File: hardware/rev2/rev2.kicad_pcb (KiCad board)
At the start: 2 copper layers, 24 parts, among them J1 Conn_01x09_Female, J2 RFM9X_header, J3 Conn_02x03_Odd_Even, U2 MPL3115A2, U3 Teensy3.6, U5 ADXL345BCCZ, U7 TPS2113ADRBR

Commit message: update netlist
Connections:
- U3 pad 11: MAIN_DEPLOY -> INT1_ADXL345
- U3 pad 12: DROGUE_DEPLOY -> INT2_ADXL345
- U3 pad 2: INT1_ADXL345 -> Net-(U3-Pad2)
- U3 pad 21: BUZZER -> INT1_MPL3115A2
- U3 pad 22: Net-(U3-Pad22) -> INT2_MPL3115A2
- U3 pad 3: INT2_ADXL345 -> Net-(U3-Pad3)
- U3 pad 35: Net-(U3-Pad35) -> BUZZER
- U3 pad 5: SCL_TEENSY -> Net-(U3-Pad5)
- U3 pad 6: SDA_TEENSY -> Net-(U3-Pad6)
- U3 pad 7: INT1_MPL3115A2 -> MAIN_DEPLOY
- U3 pad 8: INT2_MPL3115A2 -> DROGUE_DEPLOY
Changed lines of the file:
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@@
     (zones 0)
     (modules 24)
-    (nets 73)
+    (nets 75)
   )
   (page A4)
@@
   (net 55 "Net-(J1-Pad7)")
   (net 56 "Net-(J1-Pad9)")
-  (net 57 "Net-(U3-Pad35)")
-  (net 58 MAIN_DEPLOY)
-  (net 59 DROGUE_DEPLOY)
-  (net 60 3.3VBMS_Backup)
-  (net 61 "Net-(J3-Pad6)")
-  (net 62 BUZZER)
-  (net 63 "Net-(R5-Pad1)")
-  (net 64 "Net-(R7-Pad2)")
-  (net 65 "Net-(U3-Pad18)")
-  (net 66 "Net-(U3-Pad19)")
-  (net 67 "Net-(U3-Pad22)")
-  (net 68 "Net-(U3-Pad23)")
-  (net 69 "Net-(U3-Pad24)")
-  (net 70 "Net-(U3-Pad10)")
-  (net 71 "Net-(U3-Pad9)")
-  (net 72 "Net-(U7-Pad1)")
+  (net 57 MAIN_DEPLOY)
+  (net 58 DROGUE_DEPLOY)
+  (net 59 3.3VBMS_Backup)
+  (net 60 "Net-(J3-Pad6)")
+  (net 61 BUZZER)
+  (net 62 "Net-(R5-Pad1)")
+  (net 63 "Net-(R7-Pad2)")
+  (net 64 "Net-(U3-Pad18)")
+  (net 65 "Net-(U3-Pad19)")
+  (net 66 "Net-(U3-Pad23)")
+  (net 67 "Net-(U3-Pad24)")
+  (net 68 "Net-(U3-Pad10)")
+  (net 69 "Net-(U3-Pad9)")
+  (net 70 "Net-(U7-Pad1)")
+  (net 71 "Net-(U3-Pad6)")
+  (net 72 "Net-(U3-Pad5)")
+  (net 73 "Net-(U3-Pad3)")
+  (net 74 "Net-(U3-Pad2)")
   (net_class Default "This is the default net class."
     (clearance 0.2)
@@
     (add_net "Net-(U3-Pad18)")
     (add_net "Net-(U3-Pad19)")
+    (add_net "Net-(U3-Pad2)")
     (add_net "Net-(U3-Pad20)")
-    (add_net "Net-(U3-Pad22)")
     (add_net "Net-(U3-Pad23)")
     (add_net "Net-(U3-Pad24)")
@@
     (add_net "Net-(U3-Pad28)")
     (add_net "Net-(U3-Pad29)")
-    (add_net "Net-(U3-Pad35)")
+    (add_net "Net-(U3-Pad3)")
     (add_net "Net-(U3-Pad36)")
     (add_net "Net-(U3-Pad37)")
@@
     (add_net "Net-(U3-Pad47)")
     (add_net "Net-(U3-Pad48)")
+    (add_net "Net-(U3-Pad5)")
     (add_net "Net-(U3-Pad51)")
     (add_net "Net-(U3-Pad52)")
@@
     (add_net "Net-(U3-Pad56)")
     (add_net "Net-(U3-Pad57)")
+    (add_net "Net-(U3-Pad6)")
     (add_net "Net-(U3-Pad9)")
     (add_net "Net-(U5-Pad10)")
@@
       (net 29 "Net-(U3-Pad17)"))
     (pad 18 thru_hole circle (at 13.97 7.62) (size 1.6 1.6) (drill 1.1) (layers *.Cu *.Mask)
-      (net 65 "Net-(U3-Pad18)"))
+      (net 64 "Net-(U3-Pad18)"))
     (pad 19 thru_hole circle (at 16.51 7.62) (size 1.6 1.6) (drill 1.1) (layers *.Cu *.Mask)
-      (net 66 "Net-(U3-Pad19)"))
+      (net 65 "Net-(U3-Pad19)"))
     (pad 20 thru_hole circle (at 19.05 7.62) (size 1.6 1.6) (drill 1.1) (layers *.Cu *.Mask)
       (net 7 "Net-(U3-Pad20)"))
@@
       (net 43 MISO_RFM9X))
     (pad 21 thru_hole circle (at 21.59 7.62) (size 1.6 1.6) (drill 1.1) (layers *.Cu *.Mask)
-      (net 62 BUZZER))
+      (net 6 INT1_MPL3115A2))
     (pad 22 thru_hole circle (at 24.13 7.62) (size 1.6 1.6) (drill 1.1) (layers *.Cu *.Mask)
-      (net 67 "Net-(U3-Pad22)"))
+      (net 5 INT2_MPL3115A2))
     (pad 23 thru_hole circle (at 26.67 7.62) (size 1.6 1.6) (drill 1.1) (layers *.Cu *.Mask)
-      (net 68 "Net-(U3-Pad23)"))
+      (net 66 "Net-(U3-Pad23)"))
     (pad 24 thru_hole circle (at 29.21 7.62) (size 1.6 1.6) (drill 1.1) (layers *.Cu *.Mask)
-      (net 69 "Net-(U3-Pad24)"))
+      (net 67 "Net-(U3-Pad24)"))
     (pad 25 thru_hole circle (at 16.51 5.08) (size 1.6 1.6) (drill 1.1) (layers *.Cu *.Mask)
       (net 8 "Net-(U3-Pad25)"))
@@
       (net 34 PPS))
     (pad 35 thru_hole circle (at 16.51 -7.62) (size 1.6 1.6) (drill 1.1) (layers *.Cu *.Mask)
-      (net 57 "Net-(U3-Pad35)"))
+      (net 61 BUZZER))
     (pad 36 thru_hole circle (at 13.97 -7.62) (size 1.6 1.6) (drill 1.1) (layers *.Cu *.Mask)
       (net 13 "Net-(U3-Pad36)"))
@@
       (net 44 MOSI_RFM9X))
     (pad 12 thru_hole circle (at -1.27 7.62) (size 1.6 1.6) (drill 1.1) (layers *.Cu *.Mask)
-      (net 59 DROGUE_DEPLOY))
+      (net 36 INT2_ADXL345))
     (pad 11 thru_hole circle (at -3.81 7.62) (size 1.6 1.6) (drill 1.1) (layers *.Cu *.Mask)
-      (net 58 MAIN_DEPLOY))
+      (net 37 INT1_ADXL345))
     (pad 10 thru_hole circle (at -6.35 7.62) (size 1.6 1.6) (drill 1.1) (layers *.Cu *.Mask)
-      (net 70 "Net-(U3-Pad10)"))
+      (net 68 "Net-(U3-Pad10)"))
     (pad 9 thru_hole circle (at -8.89 7.62) (size 1.6 1.6) (drill 1.1) (layers *.Cu *.Mask)
-      (net 71 "Net-(U3-Pad9)"))
+      (net 69 "Net-(U3-Pad9)"))
     (pad 8 thru_hole circle (at -11.43 7.62) (size 1.6 1.6) (drill 1.1) (layers *.Cu *.Mask)
-      (net 5 INT2_MPL3115A2))
+      (net 58 DROGUE_DEPLOY))
     (pad 7 thru_hole circle (at -13.97 7.62) (size 1.6 1.6) (drill 1.1) (layers *.Cu *.Mask)
-      (net 6 INT1_MPL3115A2))
+      (net 57 MAIN_DEPLOY))
     (pad 6 thru_hole circle (at -16.51 7.62) (size 1.6 1.6) (drill 1.1) (layers *.Cu *.Mask)
-      (net 3 SDA_TEENSY))
+      (net 71 "Net-(U3-Pad6)"))
     (pad 5 thru_hole circle (at -19.05 7.62) (size 1.6 1.6) (drill 1.1) (layers *.Cu *.Mask)
-      (net 4 SCL_TEENSY))
+      (net 72 "Net-(U3-Pad5)"))
     (pad 4 thru_hole circle (at -21.59 7.62) (size 1.6 1.6) (drill 1.1) (layers *.Cu *.Mask)
       (net 41 G0_RFM9X))
     (pad 3 thru_hole circle (at -24.13 7.62) (size 1.6 1.6) (drill 1.1) (layers *.Cu *.Mask)
-      (net 36 INT2_ADXL345))
+      (net 73 "Net-(U3-Pad3)"))
     (pad 2 thru_hole circle (at -26.67 7.62) (size 1.6 1.6) (drill 1.1) (layers *.Cu *.Mask)
-      (net 37 INT1_ADXL345))
+      (net 74 "Net-(U3-Pad2)"))
     (pad 1 thru_hole rect (at -29.21 7.62) (size 1.6 1.6) (drill 1.1) (layers *.Cu *.Mask)
       (net 1 GND))
@@
     (fp_line (start -1 0.62) (end -1 -0.62) (layer F.Fab) (width 0.1))
     (pad 1 smd rect (at -0.95 0 270) (size 0.7 1.3) (layers F.Cu F.Paste F.Mask)
-      (net 63 "Net-(R5-Pad1)"))
+      (net 62 "Net-(R5-Pad1)"))
     (pad 2 smd rect (at 0.95 0 270) (size 0.7 1.3) (layers F.Cu F.Paste F.Mask)
       (net 52 3.3VBMS))
@@
       (net 1 GND))
     (pad P thru_hole circle (at 7.5 0) (size 1.71 1.71) (drill 1.14) (layers *.Cu *.Mask)
-      (net 62 BUZZER))
+      (net 61 BUZZER))
   )
   (module footprints:R_0805_OEM (layer F.Cu)
@@
       (net 1 GND))
     (pad 2 smd rect (at 0.95 0) (size 0.7 1.3) (layers F.Cu F.Paste F.Mask)
-      (net 63 "Net-(R5-Pad1)"))
+      (net 62 "Net-(R5-Pad1)"))
     (model "/home/josh/Formula/OEM_Preferred_Parts/3DModels/WRL Files/res0805.wrl"
       (at (xyz 0 0 0))
@@
     (fp_line (start 1.55 0.9) (end -1.55 0.9) (layer F.CrtYd) (width 0.05))
     (pad 2 smd rect (at 0.95 0) (size 0.7 1.3) (layers F.Cu F.Paste F.Mask)
-      (net 64 "Net-(R7-Pad2)"))
+      (net 63 "Net-(R7-Pad2)"))
     (pad 1 smd rect (at -0.95 0) (size 0.7 1.3) (layers F.Cu F.Paste F.Mask)
       (net 1 GND))
@@
       (net 54 BMS_to_Teensy))
     (pad 6 smd rect (at 1.4 0.325) (size 0.6 0.31) (layers F.Cu F.Paste)
-      (net 60 3.3VBMS_Backup))
+      (net 59 3.3VBMS_Backup))
     (pad 5 smd rect (at 1.4 0.975) (size 0.6 0.31) (layers F.Cu F.Paste)
       (net 1 GND))
     (pad 4 smd rect (at -1.4 0.975) (size 0.6 0.31) (layers F.Cu F.Paste)
-      (net 64 "Net-(R7-Pad2)"))
+      (net 63 "Net-(R7-Pad2)"))
     (pad 3 smd rect (at -1.4 0.325) (size 0.6 0.31) (layers F.Cu F.Paste)
-      (net 63 "Net-(R5-Pad1)"))
+      (net 62 "Net-(R5-Pad1)"))
     (pad 2 smd rect (at -1.4 -0.325) (size 0.6 0.31) (layers F.Cu F.Paste)
       (net 1 GND))
     (pad 1 smd rect (at -1.4 -0.975) (size 0.6 0.31) (layers F.Cu F.Paste)
-      (net 72 "Net-(U7-Pad1)"))
+      (net 70 "Net-(U7-Pad1)"))
   )
   (module Connector_PinHeader_2.54mm:PinHeader_2x03_P2.54mm_Vertical (layer F.Cu)
@@
       (net 1 GND))
     (pad 2 thru_hole oval (at 2.54 0 270) (size 1.7 1.7) (drill 1) (layers *.Cu *.Mask)
-      (net 58 MAIN_DEPLOY))
+      (net 57 MAIN_DEPLOY))
     (pad 3 thru_hole oval (at 0 2.54 270) (size 1.7 1.7) (drill 1) (layers *.Cu *.Mask)
       (net 52 3.3VBMS))
     (pad 4 thru_hole oval (at 2.54 2.54 270) (size 1.7 1.7) (drill 1) (layers *.Cu *.Mask)
-      (net 59 DROGUE_DEPLOY))
+      (net 58 DROGUE_DEPLOY))
     (pad 5 thru_hole oval (at 0 5.08 270) (size 1.7 1.7) (drill 1) (layers *.Cu *.Mask)
-      (net 60 3.3VBMS_Backup))
+      (net 59 3.3VBMS_Backup))
     (pad 6 thru_hole oval (at 2.54 5.08 270) (size 1.7 1.7) (drill 1) (layers *.Cu *.Mask)
-      (net 61 "Net-(J3-Pad6)"))
+      (net 60 "Net-(J3-Pad6)"))
     (model ${KISYS3DMOD}/Connector_PinHeader_2.54mm.3dshapes/PinHeader_2x03_P2.54mm_Vertical.wrl
       (at (xyz 0 0 0))
@@
   (via (at 154.7876 105.6132) (size 0.8) (drill 0.4) (layers F.Cu B.Cu) (net 4))
   (segment (start 154.7774 105.603) (end 154.7876 105.6132) (width 0.25) (layer F.Cu) (net 4))
-  (segment (start 133.223 102.8954) (end 133.223 102.616) (width 0.25) (layer B.Cu) (net 5) (status C00030))
+  (segment (start 133.223 102.8954) (end 133.223 102.616) (width 0.25) (layer B.Cu) (net 58) (status C00030))
   (segment (start 162.56 82.296) (end 164.846 84.582) (width 0.25) (layer F.Cu) (net 31) (status 400000))
   (segment (start 168.529 84.582) (end 171.323 87.376) (width 0.25) (layer F.Cu) (net 31) (status 800000))
@@
   (segment (start 166.751 85.09) (end 168.783 87.122) (width 0.25) (layer F.Cu) (net 35))
   (segment (start 162.814 85.09) (end 166.751 85.09) (width 0.25) (layer F.Cu) (net 35))
-  (segment (start 135.697 102.682) (end 135.763 102.616) (width 0.25) (layer B.Cu) (net 71) (status C00030))
+  (segment (start 135.697 102.682) (end 135.763 102.616) (width 0.25) (layer B.Cu) (net 69) (status C00030))
   (segment (start 118.491 82.042) (end 120.65 79.883) (width 0.25) (layer F.Cu) (net 40) (status 400010))
   (segment (start 138.43 79.883) (end 145.923 87.376) (width 0.25) (layer F.Cu) (net 40) (status 800020))

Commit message: wip
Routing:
- net GND: track 24.9 -> 42.1 mm, vias 2 -> 4
- net INT1_ADXL345: track 0.00 -> 14.2 mm, vias 0 -> 1
- net INT2_ADXL345: track 0.00 -> 11.8 mm, vias 0 -> 1
- net INT2_MPL3115A2: track 0.00 -> 6.16 mm
- net INT1_MPL3115A2: track 0.00 -> 5.62 mm
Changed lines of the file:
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@@
     (thickness 1.6)
     (drawings 18)
-    (tracks 115)
+    (tracks 143)
     (zones 0)
     (modules 24)
@@
   (segment (start 157.6451 113.8903) (end 153.7081 113.8903) (width 1) (layer F.Cu) (net 1) (status C00030))
   (segment (start 163.6549 109.4179) (end 163.6549 111.0461) (width 1) (layer F.Cu) (net 1) (status 400010))
+  (segment (start 163.6395 113.8809) (end 163.6268 113.8936) (width 1) (layer B.Cu) (net 1))
+  (segment (start 163.6395 111.0615) (end 163.6395 113.8809) (width 1) (layer B.Cu) (net 1))
+  (via (at 163.6268 113.8936) (size 1.2) (drill 0.6) (layers F.Cu B.Cu) (net 1))
+  (segment (start 163.6108 113.8776) (end 163.6268 113.8936) (width 1) (layer F.Cu) (net 1))
+  (segment (start 163.6108 113.8776) (end 161.5821 113.8903) (width 1) (layer F.Cu) (net 1) (status 800010))
+  (via (at 163.6395 111.0615) (size 1.2) (drill 0.6) (layers F.Cu B.Cu) (net 1))
   (segment (start 163.6549 111.0461) (end 163.6395 111.0615) (width 1) (layer F.Cu) (net 1))
-  (via (at 163.6395 111.0615) (size 1.2) (drill 0.6) (layers F.Cu B.Cu) (net 1))
-  (segment (start 161.5821 113.8903) (end 163.8521 113.8903) (width 1) (layer F.Cu) (net 1) (status 400010))
-  (segment (start 163.8521 113.8903) (end 163.8681 113.9063) (width 1) (layer F.Cu) (net 1))
-  (via (at 163.8681 113.9063) (size 1.2) (drill 0.6) (layers F.Cu B.Cu) (net 1))
   (segment (start 144.9545 110.5695) (end 144.78 110.744) (width 1) (layer F.Cu) (net 1))
   (segment (start 144.78 110.744) (end 144.9705 110.5535) (width 1) (layer F.Cu) (net 1))
@@
   (segment (start 142.891 110.744) (end 142.875 110.76) (width 1) (layer F.Cu) (net 1) (status C00000))
   (segment (start 142.875 110.76) (end 139.7 110.76) (width 1) (layer F.Cu) (net 1) (status C00000))
+  (segment (start 148.0125 108.3375) (end 148.9775 108.3375) (width 0.55) (layer F.Cu) (net 1) (status 400000))
+  (segment (start 151.5364 113.8936) (end 151.5397 113.8903) (width 0.55) (layer F.Cu) (net 1))
+  (via (at 151.5364 113.8936) (size 1.2) (drill 0.6) (layers F.Cu B.Cu) (net 1))
+  (segment (start 151.5364 109.728) (end 151.5364 113.8936) (width 0.55) (layer B.Cu) (net 1))
+  (via (at 150.622 108.8136) (size 1.2) (drill 0.6) (layers F.Cu B.Cu) (net 1))
+  (segment (start 149.4536 108.8136) (end 150.622 108.8136) (width 0.55) (layer F.Cu) (net 1))
+  (segment (start 148.9775 108.3375) (end 149.4536 108.8136) (width 0.55) (layer F.Cu) (net 1))
+  (segment (start 153.7081 113.8903) (end 151.5397 113.8903) (width 1) (layer F.Cu) (net 1) (status 400000))
+  (segment (start 151.5397 113.8903) (end 151.5364 113.8936) (width 1) (layer F.Cu) (net 1))
+  (segment (start 150.622 108.8136) (end 151.5364 109.728) (width 1) (layer B.Cu) (net 1))
+  (segment (start 151.5364 109.728) (end 151.5364 113.8936) (width 1) (layer B.Cu) (net 1))
   (segment (start 161.5821 112.2553) (end 167.1701 112.2553) (width 0.25) (layer F.Cu) (net 2) (status 10))
   (segment (start 169.5196 112.2553) (end 169.9006 112.6363) (width 0.25) (layer F.Cu) (net 2) (status C00030))
@@
   (via (at 154.7876 105.6132) (size 0.8) (drill 0.4) (layers F.Cu B.Cu) (net 4))
   (segment (start 154.7774 105.603) (end 154.7876 105.6132) (width 0.25) (layer F.Cu) (net 4))
+  (segment (start 164.9049 107.1679) (end 164.9049 106.4941) (width 0.25) (layer F.Cu) (net 5) (status 400000))
+  (segment (start 164.9049 106.4941) (end 168.783 102.616) (width 0.25) (layer F.Cu) (net 5) (status 800000))
+  (segment (start 163.6549 107.1679) (end 163.6549 105.2041) (width 0.25) (layer F.Cu) (net 6) (status 400000))
+  (segment (start 163.6549 105.2041) (end 166.243 102.616) (width 0.25) (layer F.Cu) (net 6) (status 800000))
   (segment (start 133.223 102.8954) (end 133.223 102.616) (width 0.25) (layer B.Cu) (net 58) (status C00030))
   (segment (start 162.56 82.296) (end 164.846 84.582) (width 0.25) (layer F.Cu) (net 31) (status 400000))
@@
   (segment (start 166.751 85.09) (end 168.783 87.122) (width 0.25) (layer F.Cu) (net 35))
   (segment (start 162.814 85.09) (end 166.751 85.09) (width 0.25) (layer F.Cu) (net 35))
+  (segment (start 148.0125 110.7375) (end 148.7489 110.7375) (width 0.25) (layer F.Cu) (net 36) (status 400000))
+  (segment (start 149.606 108.839) (end 143.383 102.616) (width 0.25) (layer B.Cu) (net 36) (status 800000))
+  (segment (start 149.606 109.8296) (end 149.606 108.839) (width 0.25) (layer B.Cu) (net 36))
+  (segment (start 148.7489 110.7375) (end 149.606 109.8804) (width 0.25) (layer F.Cu) (net 36))
+  (segment (start 149.606 109.8804) (end 149.606 109.8296) (width 0.25) (layer F.Cu) (net 36))
+  (via (at 149.606 109.8296) (size 0.8) (drill 0.4) (layers F.Cu B.Cu) (net 36))
+  (segment (start 148.0125 111.5375) (end 149.3205 111.5375) (width 0.25) (layer F.Cu) (net 37) (status 400000))
+  (segment (start 141.0716 102.616) (end 140.843 102.616) (width 0.25) (layer B.Cu) (net 37) (status C00000))
+  (segment (start 149.6568 111.2012) (end 141.0716 102.616) (width 0.25) (layer B.Cu) (net 37) (status 800000))
+  (via (at 149.6568 111.2012) (size 0.8) (drill 0.4) (layers F.Cu B.Cu) (net 37))
+  (segment (start 149.3205 111.5375) (end 149.6568 111.2012) (width 0.25) (layer F.Cu) (net 37))
   (segment (start 135.697 102.682) (end 135.763 102.616) (width 0.25) (layer B.Cu) (net 69) (status C00030))
   (segment (start 118.491 82.042) (end 120.65 79.883) (width 0.25) (layer F.Cu) (net 40) (status 400010))

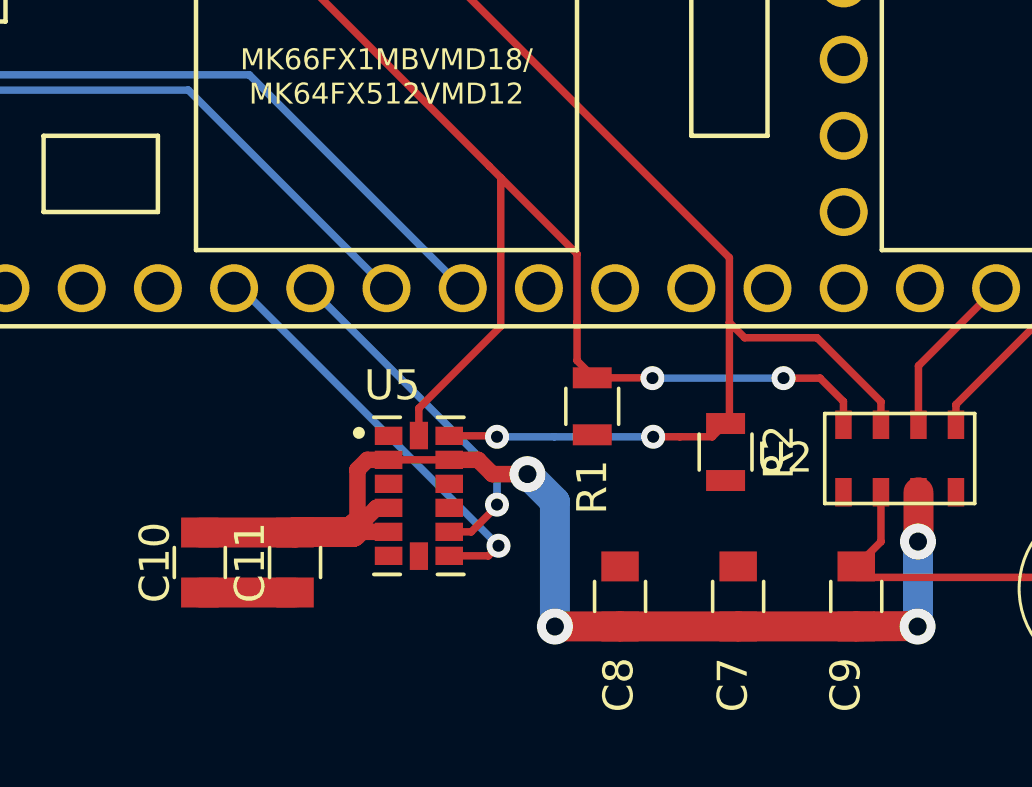
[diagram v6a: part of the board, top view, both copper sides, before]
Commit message: add 3.3V zone
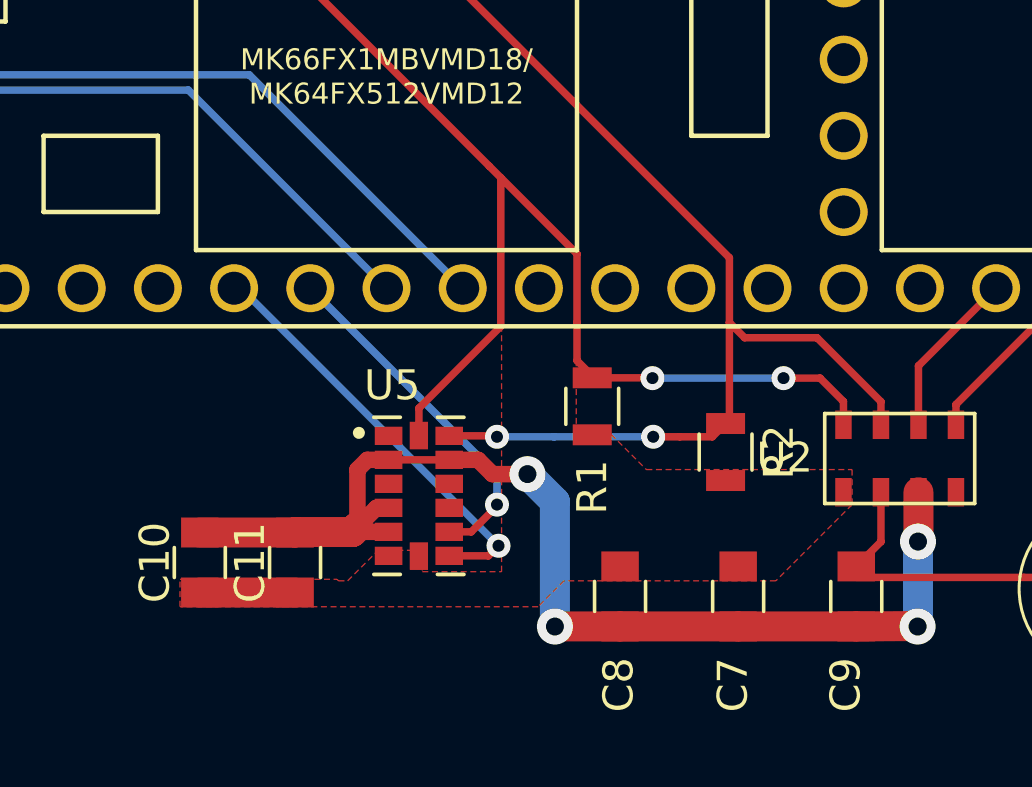
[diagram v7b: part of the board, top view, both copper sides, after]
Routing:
- added copper zone on F.Cu, net 3.3V_TEENSY
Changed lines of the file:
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@@
   (segment (start 128.651 84.328) (end 125.603 87.376) (width 0.25) (layer F.Cu) (net 46) (status 800020))
   (segment (start 139.7 112.76) (end 142.875 112.76) (width 1) (layer F.Cu) (net 53) (status C00000))
+  (zone (net 53) (net_name 3.3V_TEENSY) (layer F.Cu) (hatch edge 0.508)
+    (connect_pads (clearance 0.25))
+    (min_thickness 0.24)
+    (fill yes (arc_segments 32) (thermal_gap 0.508) (thermal_bridge_width 0.508))
+    (polygon
+      (pts
+        (xy 152.2476 101.4984) (xy 152.2476 107.4928) (xy 153.416 107.4928) (xy 154.5844 108.6612) (xy 161.4424 108.6612)
+        (xy 161.4424 109.8296) (xy 158.9024 112.3696) (xy 151.8412 112.3696) (xy 150.9776 113.2332) (xy 139.0396 113.2332)
+        (xy 139.0396 112.3188) (xy 144.272 112.3188) (xy 144.3228 112.3696) (xy 144.6276 112.3696) (xy 145.6436 111.3536)
+        (xy 146.9644 111.3536) (xy 147.1168 111.506) (xy 147.1168 112.0648) (xy 149.7584 112.0648) (xy 149.7584 99.0092)
+      )
+    )
+  )
 )

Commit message: wip
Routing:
- net 3.3V_TEENSY: track 3.18 -> 9.55 mm
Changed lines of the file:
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@@
     (thickness 1.6)
     (drawings 18)
-    (tracks 143)
+    (tracks 147)
     (zones 0)
     (modules 24)
@@
   )
   (setup
-    (last_trace_width 0.25)
+    (last_trace_width 0.55)
     (user_trace_width 0.475)
     (user_trace_width 0.55)
@@
   (segment (start 128.651 84.328) (end 125.603 87.376) (width 0.25) (layer F.Cu) (net 46) (status 800020))
   (segment (start 139.7 112.76) (end 142.875 112.76) (width 1) (layer F.Cu) (net 53) (status C00000))
+  (segment (start 151.003 102.616) (end 151.003 104.8258) (width 1) (layer F.Cu) (net 53) (status 400000))
+  (segment (start 151.4958 107.503) (end 152.781 107.503) (width 0.55) (layer F.Cu) (net 53) (status 1800000))
+  (segment (start 151.003 107.0102) (end 151.4958 107.503) (width 0.55) (layer F.Cu) (net 53) (status 1000000))
+  (segment (start 151.003 104.8258) (end 151.003 107.0102) (width 0.55) (layer F.Cu) (net 53) (status 1000000))
   (zone (net 53) (net_name 3.3V_TEENSY) (layer F.Cu) (hatch edge 0.508)
     (connect_pads (clearance 0.25))
